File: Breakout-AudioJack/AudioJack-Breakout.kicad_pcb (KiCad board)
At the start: 2 copper layers, 3 parts, among them J3 AudioJack2_Ground, J4 Conn_01x02, J8 Conn_01x02

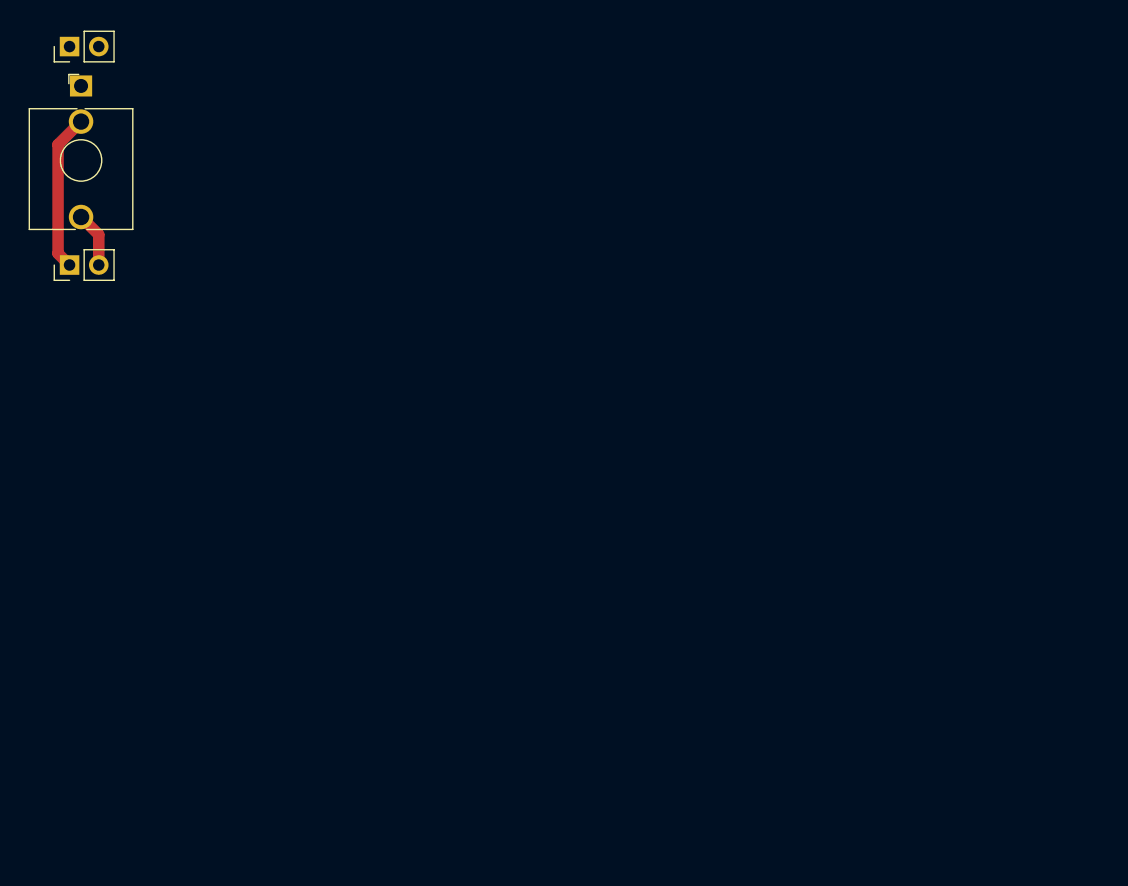
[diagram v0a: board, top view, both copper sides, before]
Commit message: Update AudioJack breakout board post fabrication issues
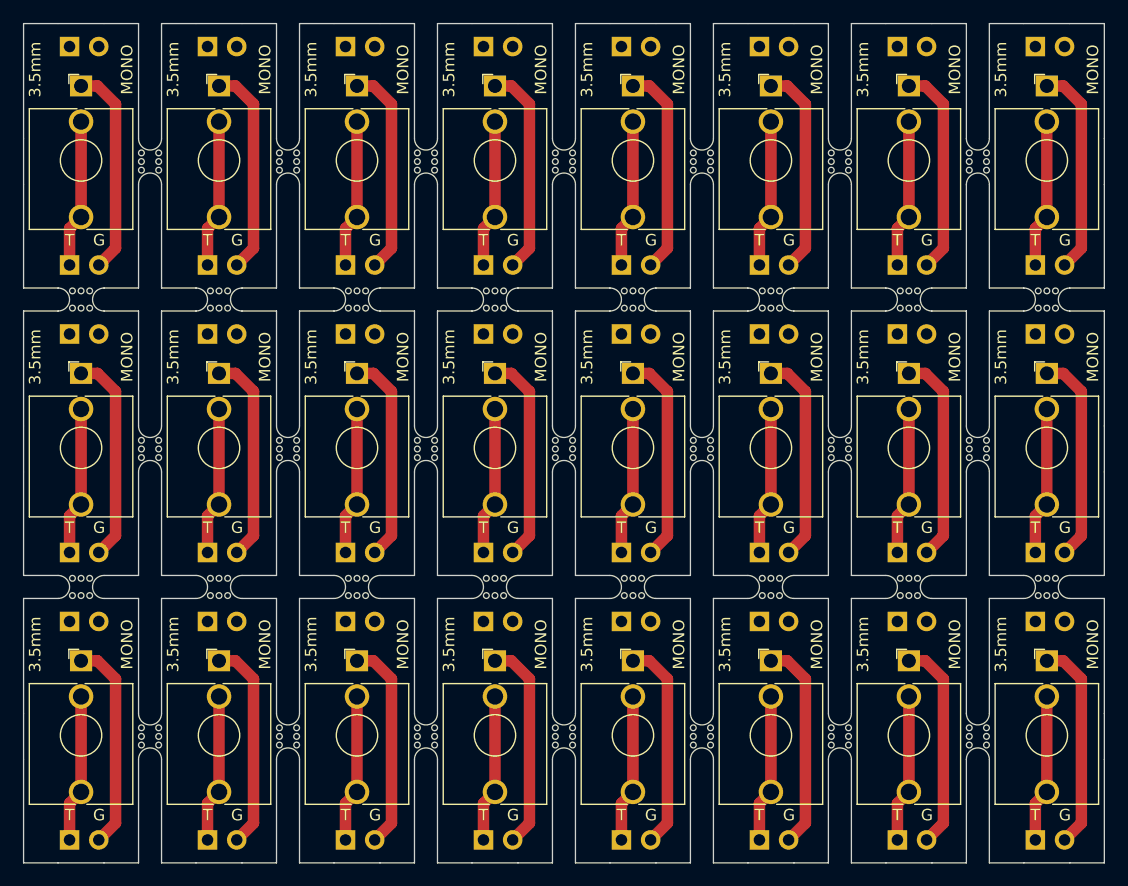
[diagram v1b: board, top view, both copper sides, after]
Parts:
- added J10: Conn_01x02, Connector_PinHeader_2.54mm:PinHeader_1x02_P2.54mm_Vertical, B.Cu at (129.0, 87.0)
- added J11: Conn_01x02, Connector_PinHeader_2.54mm:PinHeader_1x02_P2.54mm_Vertical, B.Cu at (129.0, 68.0)
- added J12: AudioJack2_Ground, LIBRARY-8-bit-computer:3.5mm-mono-jack-eurorack-2, F.Cu at (142.0, 78.0)
- added J13: Conn_01x02, Connector_PinHeader_2.54mm:PinHeader_1x02_P2.54mm_Vertical, B.Cu at (141.0, 87.0)
- added J14: Conn_01x02, Connector_PinHeader_2.54mm:PinHeader_1x02_P2.54mm_Vertical, B.Cu at (141.0, 68.0)
- added J15: AudioJack2_Ground, LIBRARY-8-bit-computer:3.5mm-mono-jack-eurorack-2, F.Cu at (154.0, 78.0)
- added J16: Conn_01x02, Connector_PinHeader_2.54mm:PinHeader_1x02_P2.54mm_Vertical, B.Cu at (153.0, 87.0)
- added J17: Conn_01x02, Connector_PinHeader_2.54mm:PinHeader_1x02_P2.54mm_Vertical, B.Cu at (153.0, 68.0)
- added J18: AudioJack2_Ground, LIBRARY-8-bit-computer:3.5mm-mono-jack-eurorack-2, F.Cu at (166.0, 78.0)
- added J19: Conn_01x02, Connector_PinHeader_2.54mm:PinHeader_1x02_P2.54mm_Vertical, B.Cu at (165.0, 87.0)
- added J20: Conn_01x02, Connector_PinHeader_2.54mm:PinHeader_1x02_P2.54mm_Vertical, B.Cu at (165.0, 68.0)
- added J21: AudioJack2_Ground, LIBRARY-8-bit-computer:3.5mm-mono-jack-eurorack-2, F.Cu at (178.0, 78.0)
- added J22: Conn_01x02, Connector_PinHeader_2.54mm:PinHeader_1x02_P2.54mm_Vertical, B.Cu at (177.0, 87.0)
- added J23: Conn_01x02, Connector_PinHeader_2.54mm:PinHeader_1x02_P2.54mm_Vertical, B.Cu at (177.0, 68.0)
- added J24: AudioJack2_Ground, LIBRARY-8-bit-computer:3.5mm-mono-jack-eurorack-2, F.Cu at (190.0, 78.0)
- added J25: Conn_01x02, Connector_PinHeader_2.54mm:PinHeader_1x02_P2.54mm_Vertical, B.Cu at (189.0, 87.0)
- added J26: Conn_01x02, Connector_PinHeader_2.54mm:PinHeader_1x02_P2.54mm_Vertical, B.Cu at (189.0, 68.0)
- added J27: AudioJack2_Ground, LIBRARY-8-bit-computer:3.5mm-mono-jack-eurorack-2, F.Cu at (106.0, 103.0)
- added J28: Conn_01x02, Connector_PinHeader_2.54mm:PinHeader_1x02_P2.54mm_Vertical, B.Cu at (105.0, 112.0)
- added J29: Conn_01x02, Connector_PinHeader_2.54mm:PinHeader_1x02_P2.54mm_Vertical, B.Cu at (105.0, 93.0)
- added J30: AudioJack2_Ground, LIBRARY-8-bit-computer:3.5mm-mono-jack-eurorack-2, F.Cu at (118.0, 103.0)
- added J31: Conn_01x02, Connector_PinHeader_2.54mm:PinHeader_1x02_P2.54mm_Vertical, B.Cu at (117.0, 112.0)
- added J32: Conn_01x02, Connector_PinHeader_2.54mm:PinHeader_1x02_P2.54mm_Vertical, B.Cu at (117.0, 93.0)
- added J33: AudioJack2_Ground, LIBRARY-8-bit-computer:3.5mm-mono-jack-eurorack-2, F.Cu at (130.0, 103.0)
- added J34: Conn_01x02, Connector_PinHeader_2.54mm:PinHeader_1x02_P2.54mm_Vertical, B.Cu at (129.0, 112.0)
- added J35: Conn_01x02, Connector_PinHeader_2.54mm:PinHeader_1x02_P2.54mm_Vertical, B.Cu at (129.0, 93.0)
- added J36: AudioJack2_Ground, LIBRARY-8-bit-computer:3.5mm-mono-jack-eurorack-2, F.Cu at (142.0, 103.0)
- added J37: Conn_01x02, Connector_PinHeader_2.54mm:PinHeader_1x02_P2.54mm_Vertical, B.Cu at (141.0, 112.0)
- added J38: Conn_01x02, Connector_PinHeader_2.54mm:PinHeader_1x02_P2.54mm_Vertical, B.Cu at (141.0, 93.0)
- added J39: AudioJack2_Ground, LIBRARY-8-bit-computer:3.5mm-mono-jack-eurorack-2, F.Cu at (154.0, 103.0)
- added J40: Conn_01x02, Connector_PinHeader_2.54mm:PinHeader_1x02_P2.54mm_Vertical, B.Cu at (153.0, 112.0)
- added J41: Conn_01x02, Connector_PinHeader_2.54mm:PinHeader_1x02_P2.54mm_Vertical, B.Cu at (153.0, 93.0)
- added J42: AudioJack2_Ground, LIBRARY-8-bit-computer:3.5mm-mono-jack-eurorack-2, F.Cu at (166.0, 103.0)
- added J43: Conn_01x02, Connector_PinHeader_2.54mm:PinHeader_1x02_P2.54mm_Vertical, B.Cu at (165.0, 112.0)
- added J44: Conn_01x02, Connector_PinHeader_2.54mm:PinHeader_1x02_P2.54mm_Vertical, B.Cu at (165.0, 93.0)
- added J45: AudioJack2_Ground, LIBRARY-8-bit-computer:3.5mm-mono-jack-eurorack-2, F.Cu at (178.0, 103.0)
- added J46: Conn_01x02, Connector_PinHeader_2.54mm:PinHeader_1x02_P2.54mm_Vertical, B.Cu at (177.0, 112.0)
- added J47: Conn_01x02, Connector_PinHeader_2.54mm:PinHeader_1x02_P2.54mm_Vertical, B.Cu at (177.0, 93.0)
- added J48: AudioJack2_Ground, LIBRARY-8-bit-computer:3.5mm-mono-jack-eurorack-2, F.Cu at (190.0, 103.0)
- added J49: Conn_01x02, Connector_PinHeader_2.54mm:PinHeader_1x02_P2.54mm_Vertical, B.Cu at (189.0, 112.0)
- added J5: AudioJack2_Ground, LIBRARY-8-bit-computer:3.5mm-mono-jack-eurorack-2, F.Cu at (118.0, 78.0)
- added J50: Conn_01x02, Connector_PinHeader_2.54mm:PinHeader_1x02_P2.54mm_Vertical, B.Cu at (189.0, 93.0)
- added J51: AudioJack2_Ground, LIBRARY-8-bit-computer:3.5mm-mono-jack-eurorack-2, F.Cu at (106.0, 128.0)
- added J52: Conn_01x02, Connector_PinHeader_2.54mm:PinHeader_1x02_P2.54mm_Vertical, B.Cu at (105.0, 137.0)
- added J53: Conn_01x02, Connector_PinHeader_2.54mm:PinHeader_1x02_P2.54mm_Vertical, B.Cu at (105.0, 118.0)
- added J54: AudioJack2_Ground, LIBRARY-8-bit-computer:3.5mm-mono-jack-eurorack-2, F.Cu at (118.0, 128.0)
- added J55: Conn_01x02, Connector_PinHeader_2.54mm:PinHeader_1x02_P2.54mm_Vertical, B.Cu at (117.0, 137.0)
- added J56: Conn_01x02, Connector_PinHeader_2.54mm:PinHeader_1x02_P2.54mm_Vertical, B.Cu at (117.0, 118.0)
- added J57: AudioJack2_Ground, LIBRARY-8-bit-computer:3.5mm-mono-jack-eurorack-2, F.Cu at (130.0, 128.0)
- added J58: Conn_01x02, Connector_PinHeader_2.54mm:PinHeader_1x02_P2.54mm_Vertical, B.Cu at (129.0, 137.0)
- added J59: Conn_01x02, Connector_PinHeader_2.54mm:PinHeader_1x02_P2.54mm_Vertical, B.Cu at (129.0, 118.0)
- added J6: Conn_01x02, Connector_PinHeader_2.54mm:PinHeader_1x02_P2.54mm_Vertical, B.Cu at (117.0, 87.0)
- added J60: AudioJack2_Ground, LIBRARY-8-bit-computer:3.5mm-mono-jack-eurorack-2, F.Cu at (142.0, 128.0)
- added J61: Conn_01x02, Connector_PinHeader_2.54mm:PinHeader_1x02_P2.54mm_Vertical, B.Cu at (141.0, 137.0)
- added J62: Conn_01x02, Connector_PinHeader_2.54mm:PinHeader_1x02_P2.54mm_Vertical, B.Cu at (141.0, 118.0)
- added J63: AudioJack2_Ground, LIBRARY-8-bit-computer:3.5mm-mono-jack-eurorack-2, F.Cu at (154.0, 128.0)
- added J64: Conn_01x02, Connector_PinHeader_2.54mm:PinHeader_1x02_P2.54mm_Vertical, B.Cu at (153.0, 137.0)
- added J65: Conn_01x02, Connector_PinHeader_2.54mm:PinHeader_1x02_P2.54mm_Vertical, B.Cu at (153.0, 118.0)
- added J66: AudioJack2_Ground, LIBRARY-8-bit-computer:3.5mm-mono-jack-eurorack-2, F.Cu at (166.0, 128.0)
- added J67: Conn_01x02, Connector_PinHeader_2.54mm:PinHeader_1x02_P2.54mm_Vertical, B.Cu at (165.0, 137.0)
- added J68: Conn_01x02, Connector_PinHeader_2.54mm:PinHeader_1x02_P2.54mm_Vertical, B.Cu at (165.0, 118.0)
- added J69: AudioJack2_Ground, LIBRARY-8-bit-computer:3.5mm-mono-jack-eurorack-2, F.Cu at (178.0, 128.0)
- added J7: AudioJack2_Ground, LIBRARY-8-bit-computer:3.5mm-mono-jack-eurorack-2, F.Cu at (130.0, 78.0)
- added J70: Conn_01x02, Connector_PinHeader_2.54mm:PinHeader_1x02_P2.54mm_Vertical, B.Cu at (177.0, 137.0)
- added J71: Conn_01x02, Connector_PinHeader_2.54mm:PinHeader_1x02_P2.54mm_Vertical, B.Cu at (177.0, 118.0)
- added J72: AudioJack2_Ground, LIBRARY-8-bit-computer:3.5mm-mono-jack-eurorack-2, F.Cu at (190.0, 128.0)
- added J73: Conn_01x02, Connector_PinHeader_2.54mm:PinHeader_1x02_P2.54mm_Vertical, B.Cu at (189.0, 137.0)
- added J74: Conn_01x02, Connector_PinHeader_2.54mm:PinHeader_1x02_P2.54mm_Vertical, B.Cu at (189.0, 118.0)
- added J9: Conn_01x02, Connector_PinHeader_2.54mm:PinHeader_1x02_P2.54mm_Vertical, B.Cu at (117.0, 68.0)
- added mouse-bite-2mm-slot1: VAL**, LIBRARY-8-bit-computer:mouse-bite-2mm-slot, F.Cu at (112.0, 78.0)
- added mouse-bite-2mm-slot1: VAL**, LIBRARY-8-bit-computer:mouse-bite-2mm-slot, F.Cu at (106.0, 90.0)
- added mouse-bite-2mm-slot10: VAL**, LIBRARY-8-bit-computer:mouse-bite-2mm-slot, F.Cu at (166.0, 90.0)
- added mouse-bite-2mm-slot11: VAL**, LIBRARY-8-bit-computer:mouse-bite-2mm-slot, F.Cu at (172.0, 78.0)
- added mouse-bite-2mm-slot12: VAL**, LIBRARY-8-bit-computer:mouse-bite-2mm-slot, F.Cu at (178.0, 90.0)
- added mouse-bite-2mm-slot13: VAL**, LIBRARY-8-bit-computer:mouse-bite-2mm-slot, F.Cu at (184.0, 78.0)
- added mouse-bite-2mm-slot14: VAL**, LIBRARY-8-bit-computer:mouse-bite-2mm-slot, F.Cu at (190.0, 90.0)
- added mouse-bite-2mm-slot16: VAL**, LIBRARY-8-bit-computer:mouse-bite-2mm-slot, F.Cu at (106.0, 115.0)
- added mouse-bite-2mm-slot17: VAL**, LIBRARY-8-bit-computer:mouse-bite-2mm-slot, F.Cu at (112.0, 103.0)
- added mouse-bite-2mm-slot18: VAL**, LIBRARY-8-bit-computer:mouse-bite-2mm-slot, F.Cu at (118.0, 115.0)
- added mouse-bite-2mm-slot19: VAL**, LIBRARY-8-bit-computer:mouse-bite-2mm-slot, F.Cu at (124.0, 103.0)
- added mouse-bite-2mm-slot2: VAL**, LIBRARY-8-bit-computer:mouse-bite-2mm-slot, F.Cu at (118.0, 90.0)
- added mouse-bite-2mm-slot20: VAL**, LIBRARY-8-bit-computer:mouse-bite-2mm-slot, F.Cu at (130.0, 115.0)
- added mouse-bite-2mm-slot21: VAL**, LIBRARY-8-bit-computer:mouse-bite-2mm-slot, F.Cu at (136.0, 103.0)
- added mouse-bite-2mm-slot22: VAL**, LIBRARY-8-bit-computer:mouse-bite-2mm-slot, F.Cu at (142.0, 115.0)
- added mouse-bite-2mm-slot23: VAL**, LIBRARY-8-bit-computer:mouse-bite-2mm-slot, F.Cu at (148.0, 103.0)
- added mouse-bite-2mm-slot24: VAL**, LIBRARY-8-bit-computer:mouse-bite-2mm-slot, F.Cu at (154.0, 115.0)
- added mouse-bite-2mm-slot25: VAL**, LIBRARY-8-bit-computer:mouse-bite-2mm-slot, F.Cu at (160.0, 103.0)
- added mouse-bite-2mm-slot26: VAL**, LIBRARY-8-bit-computer:mouse-bite-2mm-slot, F.Cu at (166.0, 115.0)
- added mouse-bite-2mm-slot27: VAL**, LIBRARY-8-bit-computer:mouse-bite-2mm-slot, F.Cu at (172.0, 103.0)
- added mouse-bite-2mm-slot28: VAL**, LIBRARY-8-bit-computer:mouse-bite-2mm-slot, F.Cu at (178.0, 115.0)
- added mouse-bite-2mm-slot29: VAL**, LIBRARY-8-bit-computer:mouse-bite-2mm-slot, F.Cu at (184.0, 103.0)
- added mouse-bite-2mm-slot3: VAL**, LIBRARY-8-bit-computer:mouse-bite-2mm-slot, F.Cu at (124.0, 78.0)
- added mouse-bite-2mm-slot30: VAL**, LIBRARY-8-bit-computer:mouse-bite-2mm-slot, F.Cu at (190.0, 115.0)
- added mouse-bite-2mm-slot33: VAL**, LIBRARY-8-bit-computer:mouse-bite-2mm-slot, F.Cu at (112.0, 128.0)
- added mouse-bite-2mm-slot35: VAL**, LIBRARY-8-bit-computer:mouse-bite-2mm-slot, F.Cu at (124.0, 128.0)
- added mouse-bite-2mm-slot37: VAL**, LIBRARY-8-bit-computer:mouse-bite-2mm-slot, F.Cu at (136.0, 128.0)
- added mouse-bite-2mm-slot39: VAL**, LIBRARY-8-bit-computer:mouse-bite-2mm-slot, F.Cu at (148.0, 128.0)
- added mouse-bite-2mm-slot4: VAL**, LIBRARY-8-bit-computer:mouse-bite-2mm-slot, F.Cu at (130.0, 90.0)
- added mouse-bite-2mm-slot41: VAL**, LIBRARY-8-bit-computer:mouse-bite-2mm-slot, F.Cu at (160.0, 128.0)
- added mouse-bite-2mm-slot43: VAL**, LIBRARY-8-bit-computer:mouse-bite-2mm-slot, F.Cu at (172.0, 128.0)
- added mouse-bite-2mm-slot45: VAL**, LIBRARY-8-bit-computer:mouse-bite-2mm-slot, F.Cu at (184.0, 128.0)
- added mouse-bite-2mm-slot5: VAL**, LIBRARY-8-bit-computer:mouse-bite-2mm-slot, F.Cu at (136.0, 78.0)
- added mouse-bite-2mm-slot6: VAL**, LIBRARY-8-bit-computer:mouse-bite-2mm-slot, F.Cu at (142.0, 90.0)
- added mouse-bite-2mm-slot7: VAL**, LIBRARY-8-bit-computer:mouse-bite-2mm-slot, F.Cu at (148.0, 78.0)
- added mouse-bite-2mm-slot8: VAL**, LIBRARY-8-bit-computer:mouse-bite-2mm-slot, F.Cu at (154.0, 90.0)
- added mouse-bite-2mm-slot9: VAL**, LIBRARY-8-bit-computer:mouse-bite-2mm-slot, F.Cu at (160.0, 78.0)
- J4, J8: moved to B.Cu
- turned J4 to -90 degrees
- turned J8 to -90 degrees
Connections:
- J3 pad G: unconnected-(J3-PadG) -> Net-(J3-PadG)
- J3 pad T: Net-(J3-PadT) -> Net-(J3-PadS)
- J4 pad 2: Net-(J3-PadT) -> Net-(J3-PadG)
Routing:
- net Net-(J3-PadG): track 0.00 -> 438.2 mm
- net Net-(J3-PadS): track 13.7 -> 309.3 mm
- net Net-(J3-PadT): track 4.81 -> 0.00 mm
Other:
- board outline added: 94 x 73 mm
- board text added: "3.5mm"
- board text added: "3.5mm Audio Jack Breakout"
- board text added: "Breadboard Compatible"
- board text added: "G"
- board text added: "MONO"
- board text added: "T"
